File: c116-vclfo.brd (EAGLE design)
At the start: 100 x 50 mm, 66 parts, among them U1 SCREW-M2X8, U10 FX2-20S-1.27DS, U11 ERM1-5MM, U2 SCREW-M2X8, U3 NUT-M2-SELFLOCK, U4 NUT-M2-SELFLOCK, U5 FX2-20P-1.27DS, U6 SCREW-M2X8, U7 SCREW-M2X8, U8 NUT-M2-SELFLOCK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

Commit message: C116 Update
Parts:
- removed VD1: BAT46, diodes-schottky:DO35-7
- added O5, O7: 450-AA150(15MM,D,BLACK), hardware:EMPTY
- added O6, O8: 450-CP151(15MM,RED/WHITE), hardware:EMPTY
- added R28, R31, R32: 100K(TH), resistors:R-0207/10
- added R29, R30: B100K(CD)(9MM), potentiometers:RV09-SINGLE
- added R33, R34: 1K8(TH), resistors:R-0207/10
- added SA5: MJS22R, switches:APEM-MJS22R
- DA2: value TL072IP -> TL074CN; device ic-ti:DIP-8 -> ic-ti:DIP-14
- HL1: value YELLOW(2MMX5MM) -> RED/GREEN(2MMX5MM,BIPOLAR)
- PCB1: device module-footprints:ST2-BOARD-50 -> module-footprints:ST2-BOARD-74
- R26, R27: value 1K8(TH) -> 100K(TH)
- SA3: value MHS233K -> MJS12R; device switches:APEM-MHS233K -> switches:APEM-MJS12R
- SA4: value MJS22R -> MHS233K; device switches:APEM-MJS22R -> switches:APEM-MHS233K
- moved SA4 86.4 mm to (83.0, 61.0), turned to 180 degrees
- moved R13 74.3 mm to (17.0, 64.0)
- moved R7 70.0 mm to (17.0, 5.00)
- moved R14 57.7 mm to (17.0, 62.0)
- moved C8 55.1 mm to (24.0, 62.0), turned to 90 degrees
- moved R20 55.1 mm to (71.5, 35.0), turned to 90 degrees
- moved R19 53.9 mm to (69.5, 35.0), turned to 90 degrees
- moved R21 53.4 mm to (74.5, 56.0), turned to 180 degrees
- moved R24 52.4 mm to (74.5, 42.0), turned to 0 degrees
- moved R16 50.7 mm to (17.0, 60.0), turned to 180 degrees
- moved R25 48.2 mm to (74.5, 54.0), turned to 0 degrees
- moved C9 46.4 mm to (67.5, 40.0)
- moved R17 46.0 mm to (60.5, 40.0)
- moved U1 45.5 mm to (78.0, -127.0)
- moved U10 45.5 mm to (105.0, -127.0)
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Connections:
- removed net N$39: DA3.12, SA3.CMN, SA4.NC1, SA4.NO2
- new net N$37: R27.2, R30.2
- new net N$42: DA2.6, R28.1, R29.3, R30.3
- new net N$44: DA2.7, R28.2, R31.1
- new net N$45: DA2.9, R29.1, R30.1, R31.2, R32.1
- new net N$46: DA2.8, DA3.12, R32.2, SA5.NC1, SA5.NO2
- new net N$47: R27.1, SA3.C
- new net N$48: R26.2, R29.2
- new net N$49: R26.1, SA4.CMN
- net +15V: now also DA2.4; no longer DA2.8
- net -15V: now also DA2.11; no longer DA2.4
- net CV1_IN: now also SA3.NO, SA5.NC2; no longer SA4.NC2
- net CV1_OUT: now also SA5.C2; no longer SA4.C2
- net CV2_IN: now also SA3.NC, SA5.NO1; no longer SA4.NO1
- net CV2_OUT: now also SA5.C1; no longer SA4.C1
- net GND: now also DA2.10, DA2.12, R33.2; no longer R26.2
- net N$22: now also SA4.1; no longer SA3.1
- net N$29: now also SA4.2; no longer SA3.2
- net N$32: now also SA4.3; no longer SA3.3
- net N$36: now also R33.1, R34.2; no longer R26.1, R27.2
- net N$40: now also HL1.A, R34.1; no longer HL1.K, R27.1, VD1.A
- net N$41: now also HL1.K; no longer HL1.A, VD1.C
- net N$7: now also DA2.13; no longer DA2.6
- net N$8: now also DA2.14; no longer DA2.7
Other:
- board size 100 x 50 mm -> 100 x 74 mm

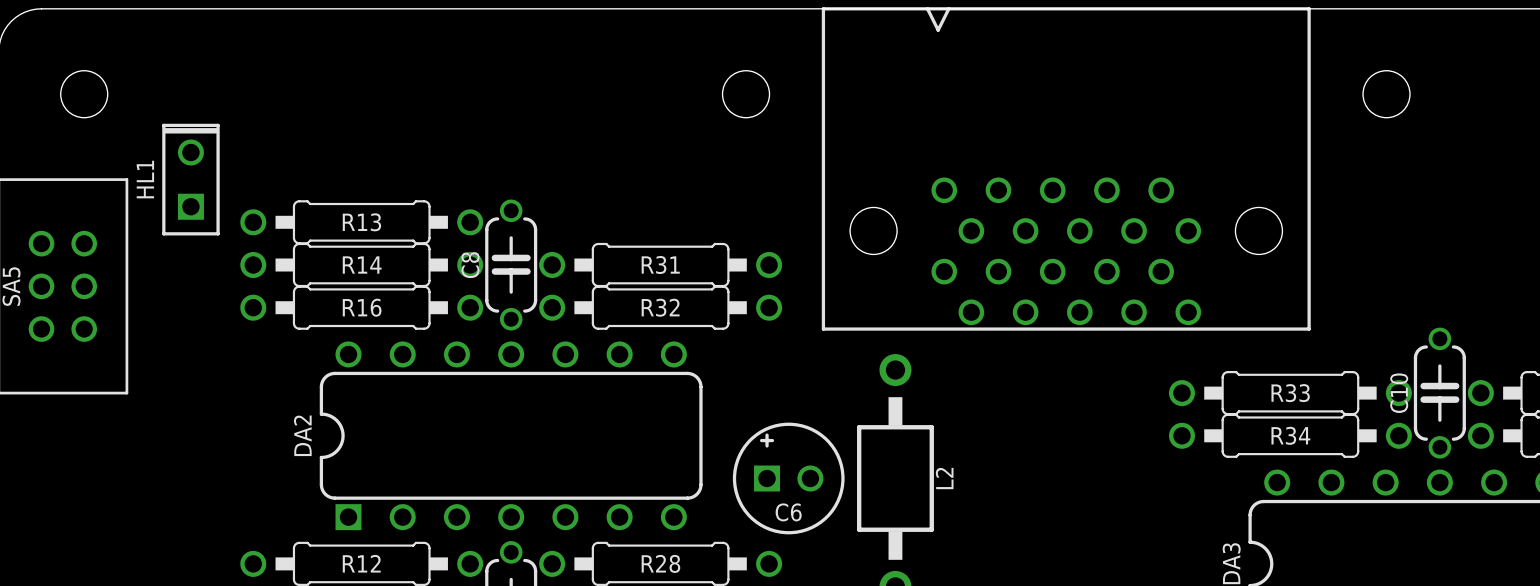
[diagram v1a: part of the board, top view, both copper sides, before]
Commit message: C116 LED circuit update
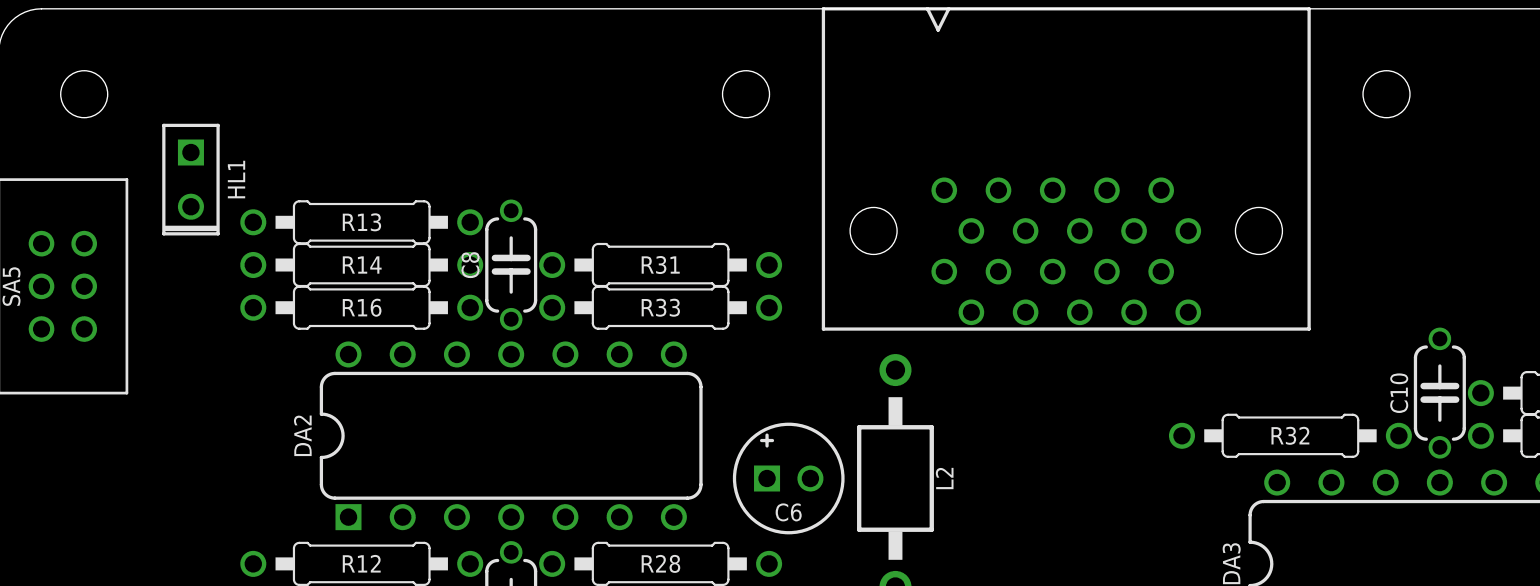
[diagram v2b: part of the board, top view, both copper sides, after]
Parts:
- removed R34: 1K8(TH), resistors:R-0207/10
- HL1: value RED/GREEN(2MMX5MM,BIPOLAR) -> WHITE(2MMX5MM)
- R32: value 100K(TH) -> 1K8(TH)
- R33: value 1K8(TH) -> 100K(TH)
- moved R32 30.1 mm to (60.5, 54.0), turned to 180 degrees
- moved R33 29.8 mm to (31.0, 60.0), turned to 0 degrees
- turned HL1 to 270 degrees
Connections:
- removed net N$40: HL1.A, R34.1
- net +15V: now also DA3.12
- net GND: no longer R33.2
- net N$36: now also HL1.A, R32.1; no longer R33.1, R34.2
- net N$45: now also R33.1; no longer R32.1
- net N$46: now also R33.2; no longer DA3.12, R32.2
- net N$49: now also R32.2
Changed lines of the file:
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@@
 <attribute name="MOUSER" value="647-USW1V100MDD" x="-6" y="-163" size="1.778" layer="27" display="off"/>
 </element>
-<element name="R33" library="resistors" package="R-0207/10" value="1K8(TH)" x="60.5" y="56" rot="R180"/>
-<element name="R34" library="resistors" package="R-0207/10" value="1K8(TH)" x="60.5" y="54"/>
+<element name="R32" library="resistors" package="R-0207/10" value="1K8(TH)" x="60.5" y="54" rot="R180"/>
 <element name="U11" library="hardware" package="EMPTY" value="ERM1-5MM" x="108" y="-127"/>
 <element name="SA3" library="switches" package="APEM-MJS12R" value="MJS12R" x="0" y="37" rot="R90">
@@
 <attribute name="MOUSER" value="71-RN55D-F-100K" x="-20" y="-184" size="1.778" layer="27" display="off"/>
 </element>
-<element name="R32" library="resistors" package="R-0207/10" value="100K(TH)" x="31" y="60">
+<element name="R33" library="resistors" package="R-0207/10" value="100K(TH)" x="31" y="60">
 <attribute name="MOUSER" value="71-RN55D-F-100K" x="-46" y="-175" size="1.778" layer="27" display="off"/>
 </element>
@@
 </element>
 <element name="O8" library="hardware" package="EMPTY" value="450-CP151(15MM,RED/WHITE)" x="75" y="-127"/>
-<element name="HL1" library="optoelectronics" package="LED2X5" value="RED/GREEN(2MMX5MM,BIPOLAR)" x="9" y="66" rot="R90"/>
 <element name="DA2" library="ic-ti" package="DIP-14" value="TL074CN" x="24" y="54"/>
+<element name="HL1" library="optoelectronics" package="LED2X5" value="WHITE(2MMX5MM)" x="9" y="66" rot="R270"/>
 </elements>
 <signals>
@@
 <contactref element="R18" pad="1"/>
 <contactref element="DA3" pad="10"/>
-<contactref element="R33" pad="2"/>
 <contactref element="DA2" pad="3"/>
 <contactref element="DA2" pad="12"/>
@@
 <contactref element="DA2" pad="10"/>
 <wire x1="70.04" y1="51.81" x2="67.5" y2="58.54" width="0" layer="19" extent="1-1"/>
-<wire x1="55.42" y1="56" x2="67.5" y2="58.54" width="0" layer="19" extent="1-1"/>
-<wire x1="53.175" y1="63.595" x2="55.42" y2="56" width="0" layer="19" extent="1-1"/>
+<wire x1="67.5" y1="37.46" x2="70.04" y2="51.81" width="0" layer="19" extent="1-1"/>
+<wire x1="67.5" y1="33.54" x2="67.5" y2="37.46" width="0" layer="19" extent="1-1"/>
+<wire x1="71.5" y1="29.92" x2="67.5" y2="33.54" width="0" layer="19" extent="1-1"/>
+<wire x1="55.42" y1="38" x2="67.5" y2="37.46" width="0" layer="19" extent="1-1"/>
+<wire x1="53.175" y1="63.595" x2="67.5" y2="58.54" width="0" layer="19" extent="1-1"/>
 <wire x1="51.905" y1="65.5" x2="53.175" y2="63.595" width="0" layer="19" extent="1-1"/>
 <wire x1="50.635" y1="63.595" x2="51.905" y2="65.5" width="0" layer="19" extent="1-1"/>
 <wire x1="49.365" y1="65.5" x2="50.635" y2="63.595" width="0" layer="19" extent="1-1"/>
 <wire x1="48.095" y1="63.595" x2="49.365" y2="65.5" width="0" layer="19" extent="1-1"/>
-<wire x1="67.5" y1="37.46" x2="70.04" y2="51.81" width="0" layer="19" extent="1-1"/>
-<wire x1="67.5" y1="33.54" x2="67.5" y2="37.46" width="0" layer="19" extent="1-1"/>
-<wire x1="71.5" y1="29.92" x2="67.5" y2="33.54" width="0" layer="19" extent="1-1"/>
-<wire x1="55.42" y1="38" x2="67.5" y2="37.46" width="0" layer="19" extent="1-1"/>
 <wire x1="35.984" y1="52" x2="48.095" y2="63.595" width="0" layer="19" extent="1-1"/>
 <wire x1="26.54" y1="50.19" x2="35.984" y2="52" width="0" layer="19" extent="1-1"/>
@@
 <contactref element="R21" pad="1"/>
 <contactref element="DA2" pad="4"/>
-<wire x1="67.5" y1="44.19" x2="79.58" y2="56" width="0" layer="19" extent="1-1"/>
+<contactref element="DA3" pad="12"/>
+<wire x1="64.96" y1="51.81" x2="79.58" y2="56" width="0" layer="19" extent="1-1"/>
+<wire x1="67.5" y1="44.19" x2="64.96" y2="51.81" width="0" layer="19" extent="1-1"/>
 <wire x1="67.5" y1="42.54" x2="67.5" y2="44.19" width="0" layer="19" extent="1-1"/>
 <wire x1="59.96" y1="32" x2="67.5" y2="42.54" width="0" layer="19" extent="1-1"/>
@@
 <signal name="N$36">
 <contactref element="DA3" pad="13"/>
-<contactref element="R33" pad="1"/>
-<contactref element="R34" pad="2"/>
-<wire x1="65.58" y1="54" x2="65.58" y2="56" width="0" layer="19" extent="1-1"/>
-<wire x1="62.42" y1="51.81" x2="65.58" y2="54" width="0" layer="19" extent="1-1"/>
+<contactref element="R32" pad="1"/>
+<contactref element="HL1" pad="A"/>
+<wire x1="62.42" y1="51.81" x2="9" y2="67.27" width="0" layer="19" extent="1-1"/>
+<wire x1="65.58" y1="54" x2="62.42" y2="51.81" width="0" layer="19" extent="1-1"/>
 </signal>
 <signal name="N$41">
 <contactref element="DA3" pad="14"/>
 <contactref element="HL1" pad="K"/>
-<wire x1="9" y1="67.27" x2="59.88" y2="51.81" width="0" layer="19" extent="1-1"/>
+<wire x1="59.88" y1="51.81" x2="9" y2="64.73" width="0" layer="19" extent="1-1"/>
 </signal>
 <signal name="N$37">
@@
 </signal>
 <signal name="N$45">
-<contactref element="R32" pad="1"/>
+<contactref element="R33" pad="1"/>
 <contactref element="R31" pad="2"/>
 <contactref element="R30" pad="1"/>
@@
 </signal>
 <signal name="N$46">
-<contactref element="R32" pad="2"/>
+<contactref element="R33" pad="2"/>
 <contactref element="SA5" pad="NO2"/>
 <contactref element="SA5" pad="NC1"/>
-<contactref element="DA3" pad="12"/>
 <contactref element="DA2" pad="8"/>
-<wire x1="36.08" y1="60" x2="64.96" y2="51.81" width="0" layer="19" extent="1-1"/>
 <wire x1="31.62" y1="57.81" x2="36.08" y2="60" width="0" layer="19" extent="1-1"/>
 <wire x1="4" y1="59" x2="31.62" y2="57.81" width="0" layer="19" extent="1-1"/>
@@
 <wire x1="29" y1="31.92" x2="32" y2="37" width="0" layer="19" extent="1-1"/>
 </signal>
-<signal name="N$40">
-<contactref element="HL1" pad="A"/>
-<contactref element="R34" pad="1"/>
-<wire x1="9" y1="64.73" x2="55.42" y2="54" width="0" layer="19" extent="1-1"/>
-</signal>
 <signal name="N$49">
 <contactref element="SA4" pad="CMN"/>
 <contactref element="R26" pad="1"/>
-<wire x1="29" y1="42.08" x2="83" y2="59.75" width="0" layer="19" extent="1-1"/>
+<contactref element="R32" pad="2"/>
+<wire x1="55.42" y1="54" x2="83" y2="59.75" width="0" layer="19" extent="1-1"/>
+<wire x1="29" y1="42.08" x2="55.42" y2="54" width="0" layer="19" extent="1-1"/>
 </signal>
 </signals>
